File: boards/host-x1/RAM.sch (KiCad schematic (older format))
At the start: 0 parts

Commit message: Continued work on power supply
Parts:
- added U2: XC7A100T-1FTG256C, symbol XC7AxT-xFTG256x
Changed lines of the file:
@@
 $Descr A4 11693 8268
 encoding utf-8
-Sheet 1 4
+Sheet 3 5
 Title "STARSHIPRAIDER Single-Lane Host"
 Date "2017-05-04"
@@
 Comment4 ""
 $EndDescr
+$Comp
+L XC7AxT-xFTG256x U2
+U 6 1 590BFFBD
+P 1750 6050
+F 0 "U2" H 3128 8558 60  0000 L CNN
+F 1 "XC7A100T-1FTG256C" H 3128 8452 60  0000 L CNN
+F 2 "" H 1750 6050 60  0000 C CNN
+F 3 "" H 1750 6050 60  0000 C CNN
+	6    1750 6050
+	1    0    0    -1
+$EndComp
+$Comp
+L XC7AxT-xFTG256x U2
+U 5 1 590C013F
+P 4850 6000
+F 0 "U2" H 6228 8508 60  0000 L CNN
+F 1 "XC7A100T-1FTG256C" H 6228 8402 60  0000 L CNN
+F 2 "" H 4850 6000 60  0000 C CNN
+F 3 "" H 4850 6000 60  0000 C CNN
+	5    4850 6000
+	1    0    0    -1
+$EndComp
 $EndSCHEMATC

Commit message: Initial work on RAM
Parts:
- added C? (x12): 0.47 uF, symbol C
- added C? (x4): 4.7 uF, symbol C
- added R? (x4): 10K, symbol R
- added U? (x4): S27KS0641, symbol S27KS0641
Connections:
- net RAM1_CLK_N: now reaches U2.A2 (IO_L8N_T1_AD14N_35)
- net RAM1_CLK_N: now also U?.B1 (CK_N)
- net RAM0_DQ3: now reaches U2.A3 (IO_L4N_T0_35)
- net RAM0_DQ3: now also U?.D4 (DQ3)
- net RAM0_DQ1: now reaches U2.A4 (IO_L3N_T0_DQS_AD5N_35)
- net RAM0_DQ1: now also U?.D2 (DQ1)
- net RAM0_DQ0: now reaches U2.A5 (IO_L3P_T0_DQS_AD5P_35)
- net RAM0_DQ0: now also U?.D3 (DQ0)
- net RAM0_CLK_N: now reaches U2.A7 (IO_L1N_T0_AD4N_35)
- net RAM0_CLK_N: now also U?.B1 (CK_N)
- net RAM1_DQ0: now reaches U2.B1 (IO_L9N_T1_DQS_AD7N_35)
- net RAM1_DQ0: now also U?.D3 (DQ0)
- net RAM1_CLK_P: now reaches U2.B2 (IO_L8P_T1_AD14P_35)
- net RAM1_CLK_P: now also U?.B2 (CK_P)
- net RAM0_DQ2: now reaches U2.B4 (IO_L4P_T0_35)
- net RAM0_DQ2: now also U?.C4 (DQ2)
- net RAM0_RST_N: now reaches U2.B5 (IO_L2N_T0_AD12N_35)
- net RAM0_RST_N: now also U?.A4 (RST_N)
- net RAM0_DQS: now reaches U2.B6 (IO_L2P_T0_AD12P_35)
- net RAM0_DQS: now also U?.C3 (DQS)
- net RAM0_CLK_P: now reaches U2.B7 (IO_L1P_T0_AD4P_35)
- net RAM0_CLK_P: now also U?.B2 (CK_P)
- net RAM1_DQS: now reaches U2.C1 (IO_L9P_T1_DQS_AD7P_35)
- net RAM1_DQS: now also U?.C3 (DQS)
- net RAM1_RST_N: now reaches U2.C2 (IO_L7N_T1_AD6N_35)
- net RAM1_RST_N: now also U?.A4 (RST_N)
- net RAM1_CS_N: now reaches U2.C3 (IO_L7P_T1_AD6P_35)
- net RAM1_CS_N: now also R?.1, U?.A3 (CS_N)
- net RAM1_DQ6: now reaches U2.C4 (IO_L12N_T1_MRCC_35)
- net RAM1_DQ6: now also U?.E2 (DQ6)
- net RAM0_DQ5: now reaches U2.C6 (IO_L5N_T0_AD13N_35)
- net RAM0_DQ5: now also U?.E3 (DQ5)
- net RAM0_DQ4: now reaches U2.C7 (IO_L5P_T0_AD13P_35)
- net RAM0_DQ4: now also U?.D5 (DQ4)
- net RAM1_DQ2: now reaches U2.D1 (IO_L10N_T1_AD15N_35)
- net RAM1_DQ2: now also U?.C4 (DQ2)
- net RAM1_DQ4: now reaches U2.D3 (IO_L11N_T1_SRCC_35)
- net RAM1_DQ4: now also U?.D5 (DQ4)
- net RAM1_DQ5: now reaches U2.D4 (IO_L12P_T1_MRCC_35)
- net RAM1_DQ5: now also U?.E3 (DQ5)
- net RAM0_DQ7: now reaches U2.D5 (IO_L6N_T0_VREF_35)
- net RAM0_DQ7: now also U?.E1 (DQ7)
- net RAM0_DQ6: now reaches U2.D6 (IO_L6P_T0_35)
- net RAM0_DQ6: now also U?.E2 (DQ6)
- net RAM2_CS_N: now reaches U2.E1 (IO_L15N_T2_DQS_35)
- net RAM2_CS_N: now also R?.1, U?.A3 (CS_N)
- net RAM1_DQ1: now reaches U2.E2 (IO_L9N_T1_DQS_AD7N_35)
- net RAM1_DQ1: now also U?.D2 (DQ1)
- net RAM1_DQ3: now reaches U2.E3 (IO_L11P_T1_SRCC_35)
- net RAM1_DQ3: now also U?.D4 (DQ3)
- net RAM2_RST_N: now reaches U2.E5 (IO_L13P_T2_MRCC_35)
- net RAM2_RST_N: now also U?.A4 (RST_N)
- net RAM0_CS_N: now reaches U2.E6 (IO_0_35)
- net RAM0_CS_N: now also R?.1, U?.A3 (CS_N)
- net RAM2_DQS: now reaches U2.F2 (IO_L15P_T2_DQS_35)
- net RAM2_DQS: now also U?.C3 (DQS)
- net RAM2_CLK_N: now reaches U2.F3 (IO_L14N_T2_SRCC_35)
- net RAM2_CLK_N: now also U?.B1 (CK_N)
- net RAM2_CLK_P: now reaches U2.F4 (IO_L14P_T2_SRCC_35)
- net RAM2_CLK_P: now also U?.B2 (CK_P)
- net RAM1_DQ7: now reaches U2.F5 (IO_L13P_T2_MRCC_35)
- net RAM1_DQ7: now also U?.E1 (DQ7)
- net RAM2_DQ3: now reaches U2.G1 (IO_L17N_T2_35)
- net RAM2_DQ3: now also U?.D4 (DQ3)
- net RAM2_DQ2: now reaches U2.G2 (IO_L17P_T2_35)
- net RAM2_DQ2: now also U?.C4 (DQ2)
- net RAM2_DQ1: now reaches U2.G4 (IO_L16N_T2_35)
- net RAM2_DQ1: now also U?.D2 (DQ1)
- net RAM2_DQ0: now reaches U2.G5 (IO_L16P_T2_35)
- net RAM2_DQ0: now also U?.D3 (DQ0)
- net RAM2_DQ5: now reaches U2.H4 (IO_L18N_T2_35)
- net RAM2_DQ5: now also U?.E3 (DQ5)
- net RAM2_DQ4: now reaches U2.H5 (IO_L18P_T2_35)
- net RAM2_DQ4: now also U?.D5 (DQ4)
- net RAM2_DQ7: now reaches U2.J4 (IO_L19N_T3_VREF_35)
- net RAM2_DQ7: now also U?.E1 (DQ7)
- net RAM2_DQ6: now reaches U2.J5 (IO_L19P_T3_35)
- net RAM2_DQ6: now also U?.E2 (DQ6)
- net RAM3_CLK_P: now reaches U2.L4 (IO_L1P_T0_34)
- net RAM3_CLK_P: now also U?.B2 (CK_P)
- net RAM3_RST_N: now reaches U2.L5 (IO_0_34)
- net RAM3_RST_N: now also U?.A4 (RST_N)
- net RAM3_CS_N: now reaches U2.M1 (IO_L2N_T0_34)
- net RAM3_CS_N: now also R?.1, U?.A3 (CS_N)
- net RAM3_DQS: now reaches U2.M2 (IO_L2P_T0_34)
- net RAM3_DQS: now also U?.C3 (DQS)
- net RAM3_CLK_N: now reaches U2.M4 (IO_L1N_T0_34)
- net RAM3_CLK_N: now also U?.B1 (CK_N)
- net RAM3_DQ6: now reaches U2.M5 (IO_L6P_T0_34)
- net RAM3_DQ6: now also U?.E2 (DQ6)
- net RAM3_DQ2: now reaches U2.N1 (IO_L4P_T0_34)
- net RAM3_DQ2: now also U?.C4 (DQ2)
- net RAM3_DQ1: now reaches U2.N2 (IO_L3N_T0_DQS_34)
- net RAM3_DQ1: now also U?.D2 (DQ1)
- net RAM3_DQ0: now reaches U2.N3 (IO_L3P_T0_DQS_34)
- net RAM3_DQ0: now also U?.D3 (DQ0)
- net RAM3_DQ7: now reaches U2.N4 (IO_L6P_T0_34)
- net RAM3_DQ7: now also U?.E1 (DQ7)
- net RAM3_DQ3: now reaches U2.P1 (IO_L4N_T0_34)
- net RAM3_DQ3: now also U?.D4 (DQ3)
- net RAM3_DQ5: now reaches U2.P3 (IO_L5N_T0_34)
- net RAM3_DQ5: now also U?.E3 (DQ5)
- net RAM3_DQ4: now reaches U2.P4 (IO_L5P_T0_34)
- net RAM3_DQ4: now also U?.D5 (DQ4)
- new net 1V8: C?.1, C?.1, C?.1, C?.1, C?.1, C?.1, C?.1, C?.1, C?.1, C?.1, C?.1, C?.1, C?.1, C?.1, C?.1, C?.1, R?.2, R?.2, R?.2, R?.2, U?.B4 (VDD), U?.B4 (VDD), U?.B4 (VDD), U?.B4 (VDD), U?.D1 (VDDQ), U?.D1 (VDDQ), U?.D1 (VDDQ), U?.D1 (VDDQ), U?.E4 (VDDQ), U?.E4 (VDDQ), U?.E4 (VDDQ), U?.E4 (VDDQ)
- new net GND: C?.2, C?.2, C?.2, C?.2, C?.2, C?.2, C?.2, C?.2, C?.2, C?.2, C?.2, C?.2, C?.2, C?.2, C?.2, C?.2, U?.B3 (VSS), U?.B3 (VSS), U?.B3 (VSS), U?.B3 (VSS), U?.C1 (VSSQ), U?.C1 (VSSQ), U?.C1 (VSSQ), U?.C1 (VSSQ), U?.E5 (VSSQ), U?.E5 (VSSQ), U?.E5 (VSSQ), U?.E5 (VSSQ)
- no-connect marks 0 -> 26
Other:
- moved on the sheet: U2E, U2F

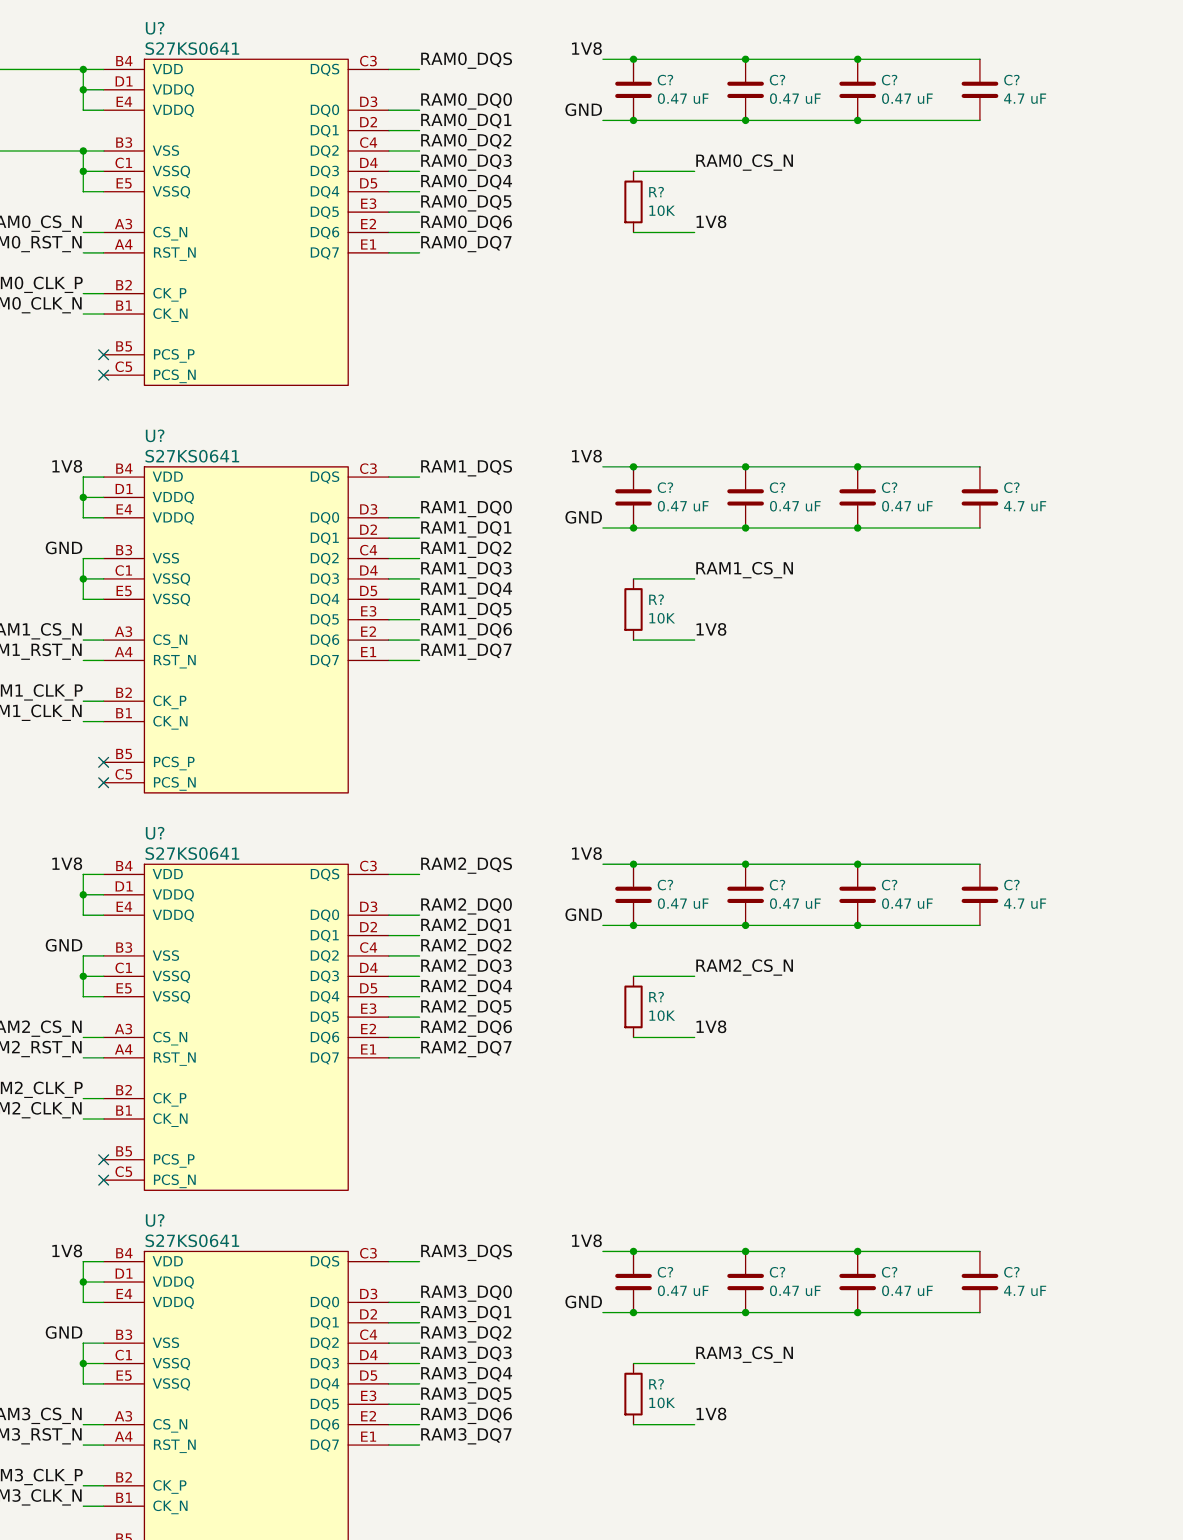
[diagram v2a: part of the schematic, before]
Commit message: Contineud work on x1 host schematic. Lots of decoupling, ethernet work, etc
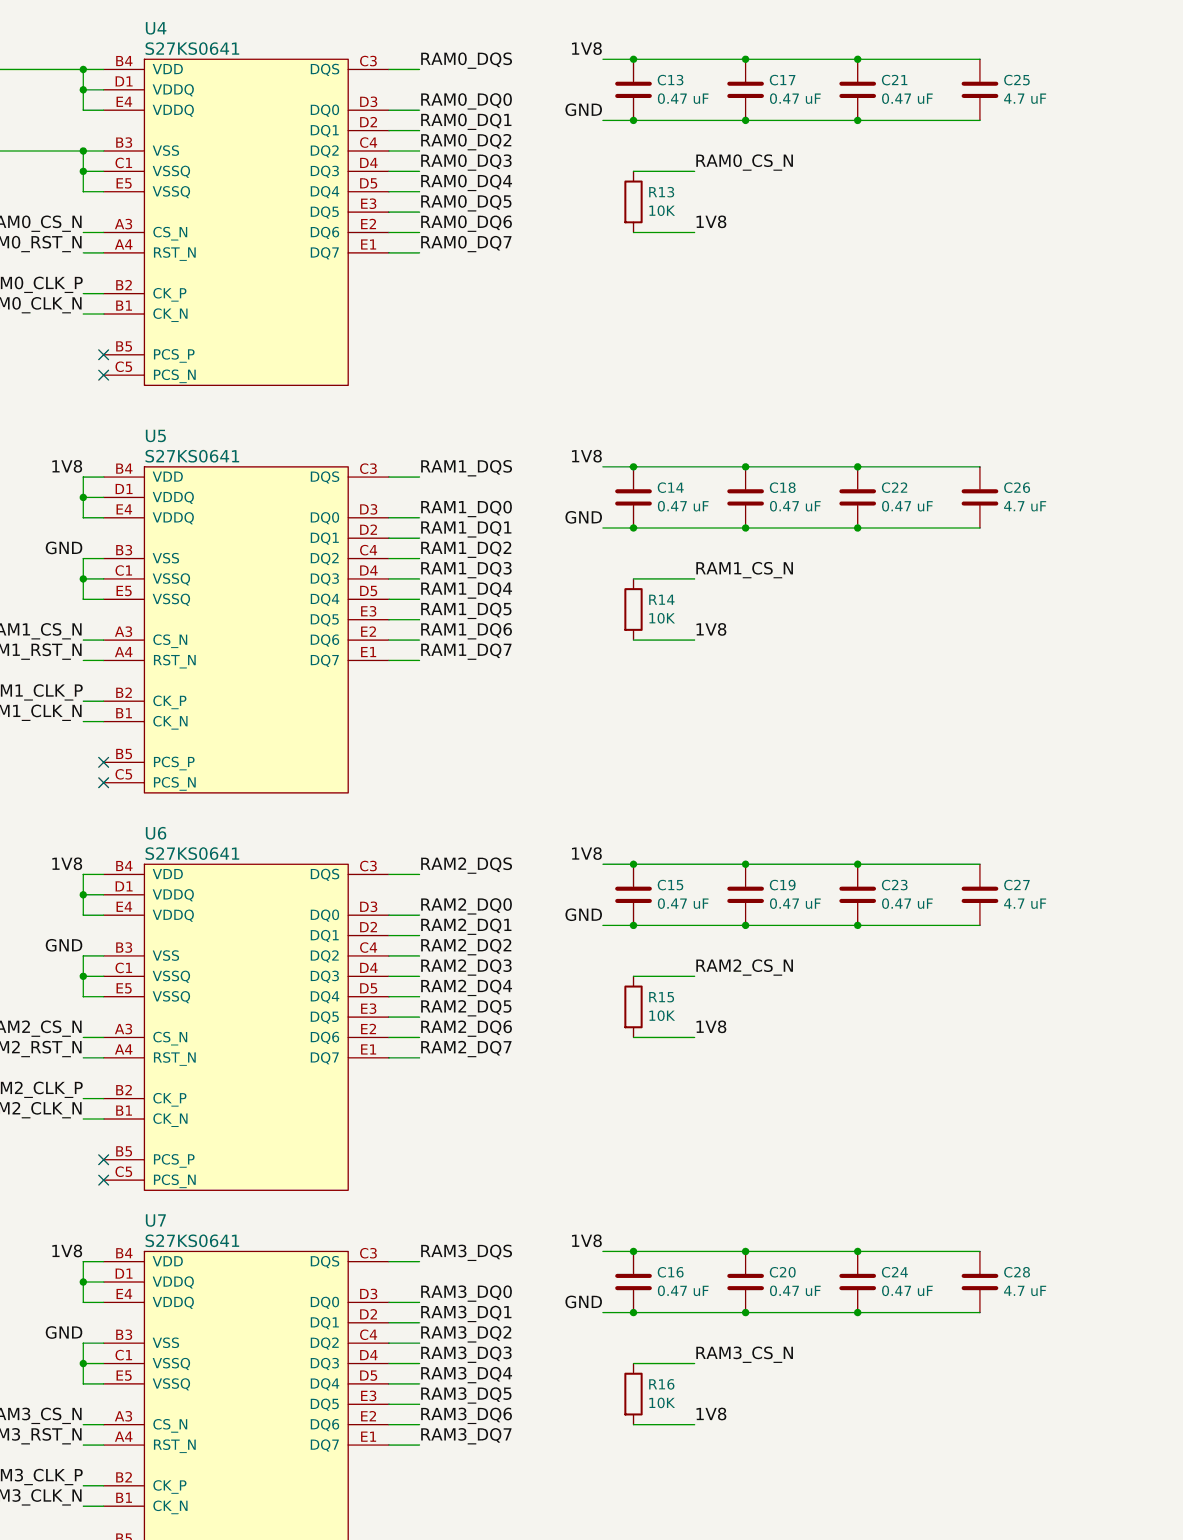
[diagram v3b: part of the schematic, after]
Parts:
- gave numbers to parts that had none: 24
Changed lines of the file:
@@
 LIBS:special-azonenberg
 LIBS:xilinx-azonenberg
+LIBS:switches
 LIBS:host-x1-cache
 EELAYER 26 0
@@
 $Descr A3 16535 11693
 encoding utf-8
-Sheet 3 5
+Sheet 3 6
 Title "STARSHIPRAIDER Single-Lane Host"
 Date "2017-05-06"
@@
 $EndComp
 $Comp
-L S27KS0641 U?
+L S27KS0641 U4
 U 1 1 590E03CD
 P 2150 2750
-F 0 "U?" H 2150 4500 60  0000 L CNN
+F 0 "U4" H 2150 4500 60  0000 L CNN
 F 1 "S27KS0641" H 2150 4400 60  0000 L CNN
 F 2 "" H 2150 2750 60  0001 C CNN
@@
 RAM0_DQ7
 $Comp
-L C C?
+L C C13
 U 1 1 590E0A6D
 P 4550 1300
-F 0 "C?" H 4665 1346 50  0000 L CNN
+F 0 "C13" H 4665 1346 50  0000 L CNN
 F 1 "0.47 uF" H 4665 1255 50  0000 L CNN
 F 2 "" H 4588 1150 50  0000 C CNN
@@
 $EndComp
 $Comp
-L C C?
+L C C17
 U 1 1 590E0BB3
 P 5100 1300
-F 0 "C?" H 5215 1346 50  0000 L CNN
+F 0 "C17" H 5215 1346 50  0000 L CNN
 F 1 "0.47 uF" H 5215 1255 50  0000 L CNN
 F 2 "" H 5138 1150 50  0000 C CNN
@@
 $EndComp
 $Comp
-L C C?
+L C C21
 U 1 1 590E0BED
 P 5650 1300
-F 0 "C?" H 5765 1346 50  0000 L CNN
+F 0 "C21" H 5765 1346 50  0000 L CNN
 F 1 "0.47 uF" H 5765 1255 50  0000 L CNN
 F 2 "" H 5688 1150 50  0000 C CNN
@@
 $EndComp
 $Comp
-L C C?
+L C C25
 U 1 1 590E0C23
 P 6250 1300
-F 0 "C?" H 6365 1346 50  0000 L CNN
+F 0 "C25" H 6365 1346 50  0000 L CNN
 F 1 "4.7 uF" H 6365 1255 50  0000 L CNN
 F 2 "" H 6288 1150 50  0000 C CNN
@@
 GND
 $Comp
-L R R?
+L R R13
 U 1 1 590E0EB1
 P 4550 1850
-F 0 "R?" H 4620 1896 50  0000 L CNN
+F 0 "R13" H 4620 1896 50  0000 L CNN
 F 1 "10K" H 4620 1805 50  0000 L CNN
 F 2 "" V 4480 1850 50  0000 C CNN
@@
 1V8
 $Comp
-L S27KS0641 U?
+L S27KS0641 U5
 U 1 1 590E12FB
 P 2150 4750
-F 0 "U?" H 2150 6500 60  0000 L CNN
+F 0 "U5" H 2150 6500 60  0000 L CNN
 F 1 "S27KS0641" H 2150 6400 60  0000 L CNN
 F 2 "" H 2150 4750 60  0001 C CNN
@@
 RAM1_DQ7
 $Comp
-L C C?
+L C C14
 U 1 1 590E132B
 P 4550 3300
-F 0 "C?" H 4665 3346 50  0000 L CNN
+F 0 "C14" H 4665 3346 50  0000 L CNN
 F 1 "0.47 uF" H 4665 3255 50  0000 L CNN
 F 2 "" H 4588 3150 50  0000 C CNN
@@
 $EndComp
 $Comp
-L C C?
+L C C18
 U 1 1 590E1331
 P 5100 3300
-F 0 "C?" H 5215 3346 50  0000 L CNN
+F 0 "C18" H 5215 3346 50  0000 L CNN
 F 1 "0.47 uF" H 5215 3255 50  0000 L CNN
 F 2 "" H 5138 3150 50  0000 C CNN
@@
 $EndComp
 $Comp
-L C C?
+L C C22
 U 1 1 590E1337
 P 5650 3300
-F 0 "C?" H 5765 3346 50  0000 L CNN
+F 0 "C22" H 5765 3346 50  0000 L CNN
 F 1 "0.47 uF" H 5765 3255 50  0000 L CNN
 F 2 "" H 5688 3150 50  0000 C CNN
@@
 $EndComp
 $Comp
-L C C?
+L C C26
 U 1 1 590E133D
 P 6250 3300
-F 0 "C?" H 6365 3346 50  0000 L CNN
+F 0 "C26" H 6365 3346 50  0000 L CNN
 F 1 "4.7 uF" H 6365 3255 50  0000 L CNN
 F 2 "" H 6288 3150 50  0000 C CNN
@@
 GND
 $Comp
-L R R?
+L R R14
 U 1 1 590E134D
 P 4550 3850
-F 0 "R?" H 4620 3896 50  0000 L CNN
+F 0 "R14" H 4620 3896 50  0000 L CNN
 F 1 "10K" H 4620 3805 50  0000 L CNN
 F 2 "" V 4480 3850 50  0000 C CNN
@@
 GND
 $Comp
-L S27KS0641 U?
+L S27KS0641 U6
 U 1 1 590E1D49
 P 2150 6700
-F 0 "U?" H 2150 8450 60  0000 L CNN
+F 0 "U6" H 2150 8450 60  0000 L CNN
 F 1 "S27KS0641" H 2150 8350 60  0000 L CNN
 F 2 "" H 2150 6700 60  0001 C CNN
@@
 RAM2_DQ7
 $Comp
-L C C?
+L C C15
 U 1 1 590E1D73
 P 4550 5250
-F 0 "C?" H 4665 5296 50  0000 L CNN
+F 0 "C15" H 4665 5296 50  0000 L CNN
 F 1 "0.47 uF" H 4665 5205 50  0000 L CNN
 F 2 "" H 4588 5100 50  0000 C CNN
@@
 $EndComp
 $Comp
-L C C?
+L C C19
 U 1 1 590E1D79
 P 5100 5250
-F 0 "C?" H 5215 5296 50  0000 L CNN
+F 0 "C19" H 5215 5296 50  0000 L CNN
 F 1 "0.47 uF" H 5215 5205 50  0000 L CNN
 F 2 "" H 5138 5100 50  0000 C CNN
@@
 $EndComp
 $Comp
-L C C?
+L C C23
 U 1 1 590E1D7F
 P 5650 5250
-F 0 "C?" H 5765 5296 50  0000 L CNN
+F 0 "C23" H 5765 5296 50  0000 L CNN
 F 1 "0.47 uF" H 5765 5205 50  0000 L CNN
 F 2 "" H 5688 5100 50  0000 C CNN
@@
 $EndComp
 $Comp
-L C C?
+L C C27
 U 1 1 590E1D85
 P 6250 5250
-F 0 "C?" H 6365 5296 50  0000 L CNN
+F 0 "C27" H 6365 5296 50  0000 L CNN
 F 1 "4.7 uF" H 6365 5205 50  0000 L CNN
 F 2 "" H 6288 5100 50  0000 C CNN
@@
 GND
 $Comp
-L R R?
+L R R15
 U 1 1 590E1D95
 P 4550 5800
-F 0 "R?" H 4620 5846 50  0000 L CNN
+F 0 "R15" H 4620 5846 50  0000 L CNN
 F 1 "10K" H 4620 5755 50  0000 L CNN
 F 2 "" V 4480 5800 50  0000 C CNN
@@
 GND
 $Comp
-L S27KS0641 U?
+L S27KS0641 U7
 U 1 1 590E24D3
 P 2150 8600
-F 0 "U?" H 2150 10350 60  0000 L CNN
+F 0 "U7" H 2150 10350 60  0000 L CNN
 F 1 "S27KS0641" H 2150 10250 60  0000 L CNN
 F 2 "" H 2150 8600 60  0001 C CNN
@@
 RAM3_DQ7
 $Comp
-L C C?
+L C C16
 U 1 1 590E24FD
 P 4550 7150
-F 0 "C?" H 4665 7196 50  0000 L CNN
+F 0 "C16" H 4665 7196 50  0000 L CNN
 F 1 "0.47 uF" H 4665 7105 50  0000 L CNN
 F 2 "" H 4588 7000 50  0000 C CNN
@@
 $EndComp
 $Comp
-L C C?
+L C C20
 U 1 1 590E2503
 P 5100 7150
-F 0 "C?" H 5215 7196 50  0000 L CNN
+F 0 "C20" H 5215 7196 50  0000 L CNN
 F 1 "0.47 uF" H 5215 7105 50  0000 L CNN
 F 2 "" H 5138 7000 50  0000 C CNN
@@
 $EndComp
 $Comp
-L C C?
+L C C24
 U 1 1 590E2509
 P 5650 7150
-F 0 "C?" H 5765 7196 50  0000 L CNN
+F 0 "C24" H 5765 7196 50  0000 L CNN
 F 1 "0.47 uF" H 5765 7105 50  0000 L CNN
 F 2 "" H 5688 7000 50  0000 C CNN
@@
 $EndComp
 $Comp
-L C C?
+L C C28
 U 1 1 590E250F
 P 6250 7150
-F 0 "C?" H 6365 7196 50  0000 L CNN
+F 0 "C28" H 6365 7196 50  0000 L CNN
 F 1 "4.7 uF" H 6365 7105 50  0000 L CNN
 F 2 "" H 6288 7000 50  0000 C CNN
@@
 GND
 $Comp
-L R R?
+L R R16
 U 1 1 590E251F
 P 4550 7700
-F 0 "R?" H 4620 7746 50  0000 L CNN
+F 0 "R16" H 4620 7746 50  0000 L CNN
 F 1 "10K" H 4620 7655 50  0000 L CNN
 F 2 "" V 4480 7700 50  0000 C CNN
